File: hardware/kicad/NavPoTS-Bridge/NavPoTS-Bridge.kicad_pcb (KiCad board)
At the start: 2 copper layers, 58.9 x 58.9 mm, 74 parts, among them J1 Conn_01x06_Pin, J2 USB_C_Receptacle_USB2.0_16P, J3 Screw_Terminal_01x06, J4 Conn_02x04_Top_Bottom, J5 Conn_02x04_Top_Bottom, J6 Conn_02x04_Top_Bottom, J7 62684-402100ALF, J8 62684-402100ALF, J9 Conn_02x04_Top_Bottom, U1 MS5611-01BA, U2 H3LIS331DLTR, U3 ASM330LHHXTR, U4 MMC5983MA, U5 USBLC6-2SC6, U6 STM32H743ZITx, Y1 ECS-2520MV-xxx-xx

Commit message: remaped pins and renamed pcb sections
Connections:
- J7 pad 06: EXT_PWR4 -> EXT_PWR2
- J7 pad 07: EXT_PWR5 -> I2C1_SDA
- J7 pad 08: I2C1_SDA -> I2C1_SCL
- J7 pad 09: I2C1_SCL -> PYRO0_FIRE
- J7 pad 10: PYRO0_FIRE -> PYRO0_CONTINUITY
- J7 pad 11: PYRO0_CONTINUITY -> PYRO1_FIRE
- J7 pad 12: PYRO1_FIRE -> PYRO1_CONTINUITY
- J7 pad 13: PYRO1_CONTINUITY -> PYRO2_FIRE
- J7 pad 14: PYRO2_FIRE -> PYRO2_CONTINUITY
- J7 pad 15: PYRO2_CONTINUITY -> PYRO3_FIRE
- J7 pad 16: PYRO3_FIRE -> PYRO3_CONTINUITY
- J7 pad 17: PYRO3_CONTINUITY -> EXT_PWR3
- J7 pad 18: PWM_0 -> EXT_PWR4
- J7 pad 19: PWM_1 -> EXT_PWR5
- J7 pad 20: PWM_2 -> PWM_0
- J7 pad 21: PWM_3 -> PWM_1
- J7 pad 22: PWM_4 -> PWM_2
- J7 pad 23: PWM_5 -> PWM_3
- J7 pad 24: PWM_6 -> PWM_4
- J7 pad 25: PWM_7 -> PWM_5
- J7 pad 26: EXT_PWR2 -> PWM_6
- J7 pad 27: EXT_PWR3 -> PWM_7
- U6 pad 26: unconnected-(U6-PC0-Pad26) -> EXT_PWR3
- U6 pad 27: unconnected-(U6-PC1-Pad27) -> EXT_PWR4
- U6 pad 28: unconnected-(U6-PC2_C-Pad28) -> EXT_PWR5
- U6 pad 56: EXT_PWR2 -> unconnected-(U6-PG0-Pad56)
- U6 pad 57: EXT_PWR3 -> unconnected-(U6-PG1-Pad57)
- U6 pad 7: EXT_PWR4 -> EXT_PWR2
- U6 pad 8: EXT_PWR5 -> unconnected-(U6-PC14-Pad8)

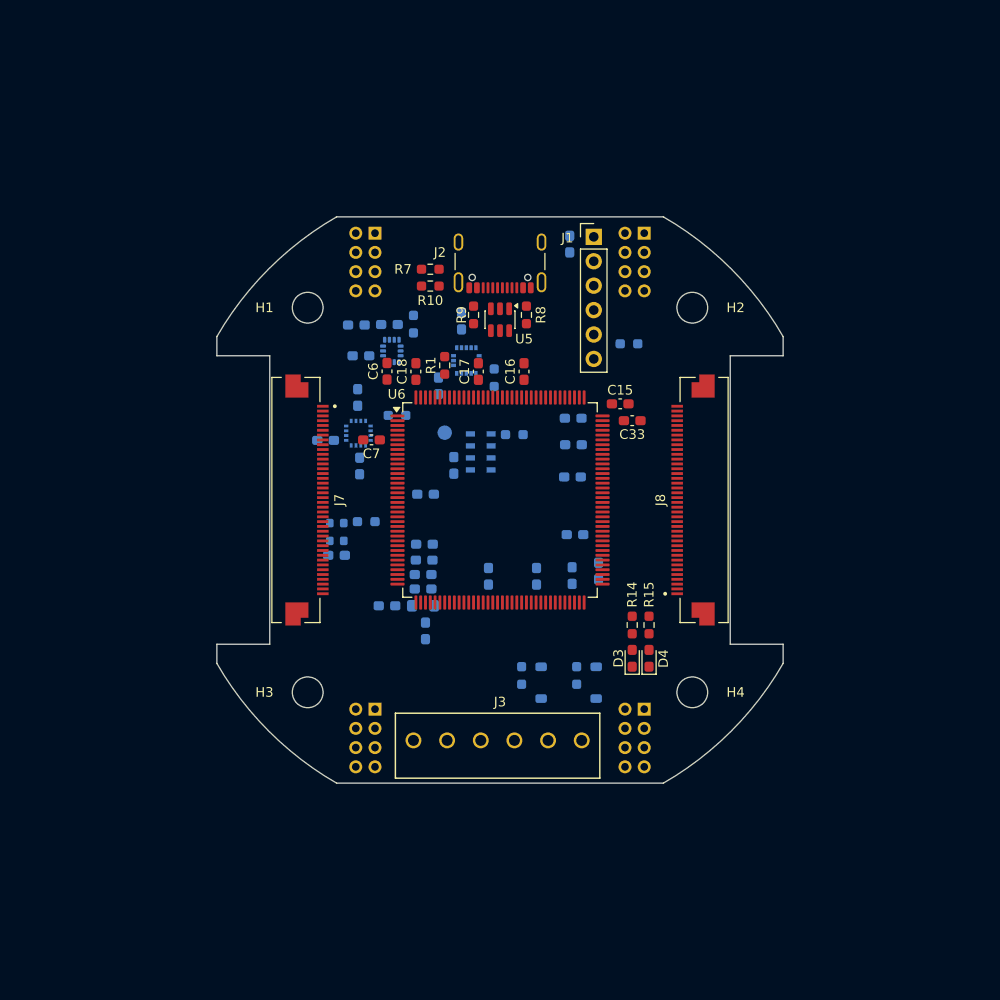
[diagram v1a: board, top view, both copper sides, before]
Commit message: first draft of bridge pcb
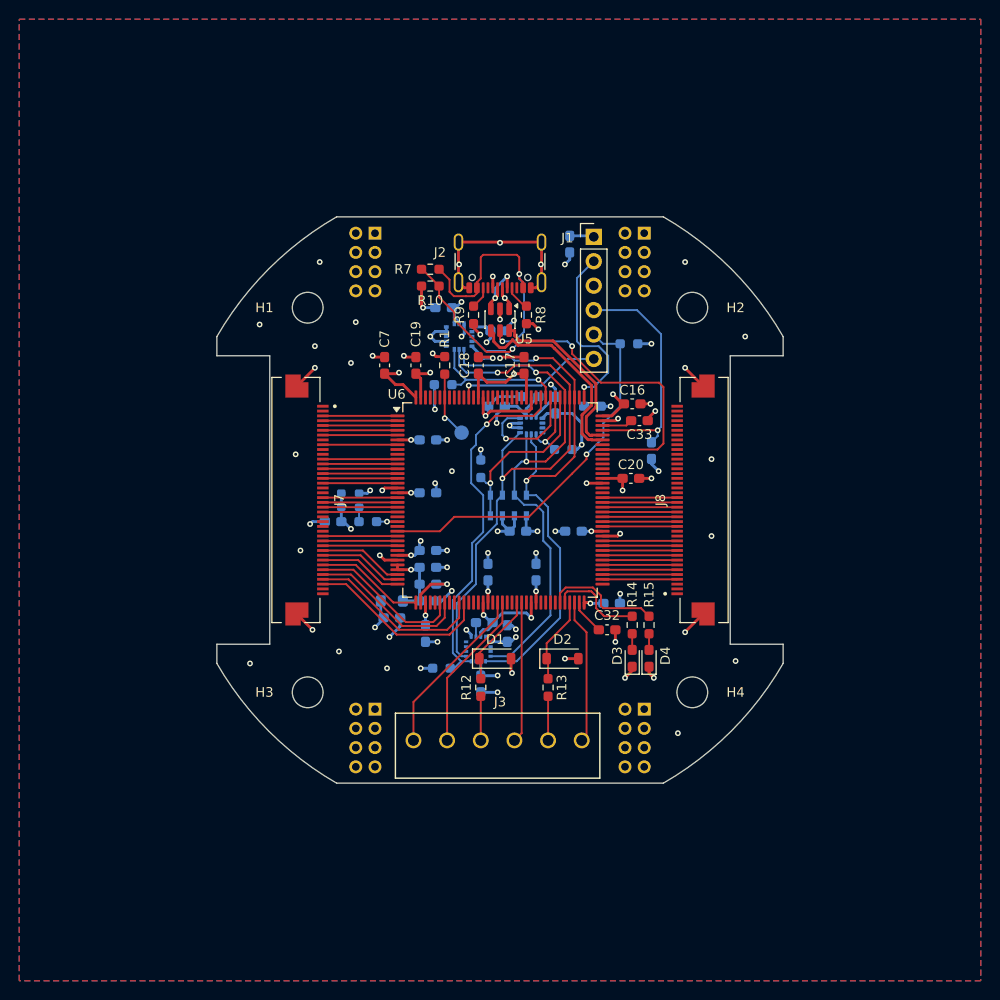
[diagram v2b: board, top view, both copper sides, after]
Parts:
- C20: renamed from C19; moved to F.Cu
- C32, D1, D2, R12, R13: moved to F.Cu
- C8: renamed from C7; moved to B.Cu
- moved C28 32.4 mm to (198.0, 119.1), turned to -90 degrees
- moved C29 27.6 mm to (200.8, 113.9), turned to 90 degrees
- moved R6 26.7 mm to (193.9, 117.5), turned to 0 degrees
- moved U4 25.7 mm to (197.8, 115.5), turned to 90 degrees
- moved C31 20.8 mm to (198.4, 112.8), turned to 0 degrees
- moved R2 20.3 mm to (206.6, 94.8), turned to 180 degrees
- moved C3 19.6 mm to (203.1, 89.2)
- moved C1 19.2 mm to (205.8, 90.1), turned to 90 degrees
- moved U3 16.4 mm to (203.2, 92.2), turned to 0 degrees
- moved C2 15.0 mm to (199.6, 90.2)
- moved C6 9.56 mm to (201.9, 103.2), turned to 180 degrees
- moved C4 8.16 mm to (194.1, 80.0), turned to 180 degrees
- moved C26 8.14 mm to (215.8, 94.9), turned to -90 degrees
- moved C32 6.71 mm to (211.1, 113.5), turned to 180 degrees
- moved U1 6.27 mm to (200.9, 100.6), turned to 90 degrees
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- renumbered C9 to C10, C10 to C11, C11 to C12, C12 to C13, C13 to C14, C14 to C15, C15 to C16, C16 to C17, C17 to C18, C18 to C19, C20 to C21, C21 to C22, C22 to C23, C26 to C25, C27 to C26, C25 to C27, C23 to C6, C6 to C7, C8 to C9
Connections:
- D1 pad 1: UART8_RX -> UART7_RX
- D2 pad 1: UART4_RX -> USART3_TX
- J3 pad 3: UART8_TX -> Net-(J3-Pin_3)
- J3 pad 4: Net-(J3-Pin_4) -> UART7_TX
- J3 pad 5: UART4_TX -> Net-(J3-Pin_5)
- J3 pad 6: Net-(J3-Pin_6) -> USART3_RX
- J7 pad 01: V_ALERT -> unconnected-(J7-Pad01)
- J7 pad 02: PGOOD -> unconnected-(J7-Pad02)
- J7 pad 03: VSTAT -> V_ALERT
- J7 pad 04: EXT_PWR0 -> PGOOD
- J7 pad 05: EXT_PWR1 -> VSTAT
- J7 pad 06: EXT_PWR2 -> EXT_PWR0
- J7 pad 07: I2C1_SDA -> EXT_PWR1
- J7 pad 08: I2C1_SCL -> unconnected-(J7-Pad08)
- J7 pad 09: PYRO0_FIRE -> EXT_PWR2
- J7 pad 10: PYRO0_CONTINUITY -> unconnected-(J7-Pad10)
- J7 pad 11: PYRO1_FIRE -> unconnected-(J7-Pad11)
- J7 pad 12: PYRO1_CONTINUITY -> I2C1_SDA
- J7 pad 13: PYRO2_FIRE -> I2C1_SCL
- J7 pad 14: PYRO2_CONTINUITY -> PYRO0_FIRE
- J7 pad 15: PYRO3_FIRE -> PYRO0_CONTINUITY
- J7 pad 16: PYRO3_CONTINUITY -> PYRO1_FIRE
- J7 pad 17: EXT_PWR3 -> PYRO1_CONTINUITY
- J7 pad 18: EXT_PWR4 -> unconnected-(J7-Pad18)
- J7 pad 19: EXT_PWR5 -> unconnected-(J7-Pad19)
- J7 pad 20: PWM_0 -> PYRO2_FIRE
- J7 pad 21: PWM_1 -> PYRO2_CONTINUITY
- J7 pad 22: PWM_2 -> PYRO3_FIRE
- J7 pad 23: PWM_3 -> PYRO3_CONTINUITY
- J7 pad 24: PWM_4 -> unconnected-(J7-Pad24)
- J7 pad 25: PWM_5 -> unconnected-(J7-Pad25)
- J7 pad 26: PWM_6 -> unconnected-(J7-Pad26)
- J7 pad 27: PWM_7 -> unconnected-(J7-Pad27)
- J7 pad 28: unconnected-(J7-Pad28) -> EXT_PWR3
- J7 pad 29: unconnected-(J7-Pad29) -> EXT_PWR4
- J7 pad 30: unconnected-(J7-Pad30) -> EXT_PWR5
- J7 pad 31: unconnected-(J7-Pad31) -> PWM_0
- J7 pad 32: unconnected-(J7-Pad32) -> PWM_1
- J7 pad 33: unconnected-(J7-Pad33) -> PWM_2
- J7 pad 34: unconnected-(J7-Pad34) -> PWM_3
- J7 pad 35: unconnected-(J7-Pad35) -> PWM_4
- J7 pad 36: unconnected-(J7-Pad36) -> PWM_5
- J7 pad 37: unconnected-(J7-Pad37) -> PWM_6
- J7 pad 38: unconnected-(J7-Pad38) -> PWM_7
- J8 pad 01: SPI2_SCK -> unconnected-(J8-Pad01)
- J8 pad 02: SPI2_MISO -> unconnected-(J8-Pad02)
- J8 pad 03: SPI2_MOSI -> unconnected-(J8-Pad03)
- J8 pad 04: SPI2_CS0 -> SPI2_SCK
- J8 pad 05: SPI2_CS1 -> SPI2_MISO
- J8 pad 06: SPI2_CS2 -> SPI2_MOSI
- J8 pad 07: SPI2_CS3 -> SPI2_CS0
- J8 pad 08: GNSS_nRST -> SPI2_CS1
- J8 pad 09: LoRa_RXEN -> SPI2_CS2
- J8 pad 10: LoRa_BUSY -> SPI2_CS3
- J8 pad 11: LoRa_IO -> GNSS_nRST
- J8 pad 12: LoRa_nRST -> LoRa_RXEN
- J8 pad 13: DEBUG_2 -> unconnected-(J8-Pad13)
- J8 pad 14: DEBUG_3 -> unconnected-(J8-Pad14)
- J8 pad 15: DEBUG_4 -> LoRa_BUSY
- J8 pad 16: DEBUG_5 -> LoRa_IO
- J8 pad 17: unconnected-(J8-Pad17) -> LoRa_nRST
- J8 pad 18: unconnected-(J8-Pad18) -> DEBUG_2
- J8 pad 19: unconnected-(J8-Pad19) -> DEBUG_3
- J8 pad 20: unconnected-(J8-Pad20) -> DEBUG_4
- J8 pad 21: unconnected-(J8-Pad21) -> DEBUG_5
- R12 pad 1: UART8_RX -> UART7_RX
- R12 pad 2: Net-(J3-Pin_4) -> Net-(J3-Pin_3)
- R13 pad 1: UART4_RX -> USART3_TX
- R13 pad 2: Net-(J3-Pin_6) -> Net-(J3-Pin_5)
- U6 pad 124: DEBUG_0 -> unconnected-(U6-PG9-Pad124)
- U6 pad 125: DEBUG_1 -> unconnected-(U6-PG10-Pad125)
- U6 pad 136: I2C4_SCL -> unconnected-(U6-PB6-Pad136)
- U6 pad 137: I2C4_SDA -> unconnected-(U6-PB7-Pad137)
- U6 pad 139: UART4_RX -> unconnected-(U6-PB8-Pad139)
- U6 pad 140: UART4_TX -> unconnected-(U6-PB9-Pad140)
- U6 pad 141: UART8_RX -> unconnected-(U6-PE0-Pad141)
- U6 pad 142: UART8_TX -> unconnected-(U6-PE1-Pad142)
- U6 pad 54: unconnected-(U6-PF14-Pad54) -> I2C4_SCL
- U6 pad 55: unconnected-(U6-PF15-Pad55) -> I2C4_SDA
- U6 pad 58: unconnected-(U6-PE7-Pad58) -> UART7_RX
- U6 pad 59: unconnected-(U6-PE8-Pad59) -> UART7_TX
- U6 pad 67: unconnected-(U6-PE14-Pad67) -> DEBUG_1
- U6 pad 68: unconnected-(U6-PE15-Pad68) -> DEBUG_0
- U6 pad 69: unconnected-(U6-PB10-Pad69) -> USART3_TX
- U6 pad 70: unconnected-(U6-PB11-Pad70) -> USART3_RX
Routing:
- net GND: track 0.00 -> 144.1 mm, vias 0 -> 75
- net +3V3: track 0.00 -> 96.3 mm, vias 0 -> 27
- net SPI3_SCK: track 0.00 -> 57.9 mm, vias 0 -> 2
- net SPI3_MISO: track 0.00 -> 56.3 mm, vias 0 -> 2
- net SPI3_MOSI: track 0.00 -> 53.3 mm, vias 0 -> 2
- net VUSB: track 0.00 -> 45.2 mm, vias 0 -> 2
- net NRST: track 0.00 -> 39.4 mm, vias 0 -> 1
- net SPI3_CS3: track 0.00 -> 37.4 mm, vias 0 -> 1
- net Net-(U5-VBUS): track 0.00 -> 27.5 mm, vias 0 -> 2
- net SWDIO: track 0.00 -> 25.4 mm, vias 0 -> 1
- net USB_D-: track 0.00 -> 21.8 mm
- net SWCLK: track 0.00 -> 20.9 mm, vias 0 -> 1
- net PWM_7: track 0.00 -> 19.3 mm
- net USB_D+: track 0.00 -> 18.9 mm
- net SPI3_CS0: track 0.00 -> 18.6 mm, vias 0 -> 1
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- added copper zone on In2.Cu, net +3V3
- added copper zone on B.Cu, net GND
- added copper zone on F.Cu, net GND
- added copper zone on In1.Cu, net GND
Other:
- copper layers 2 -> 4

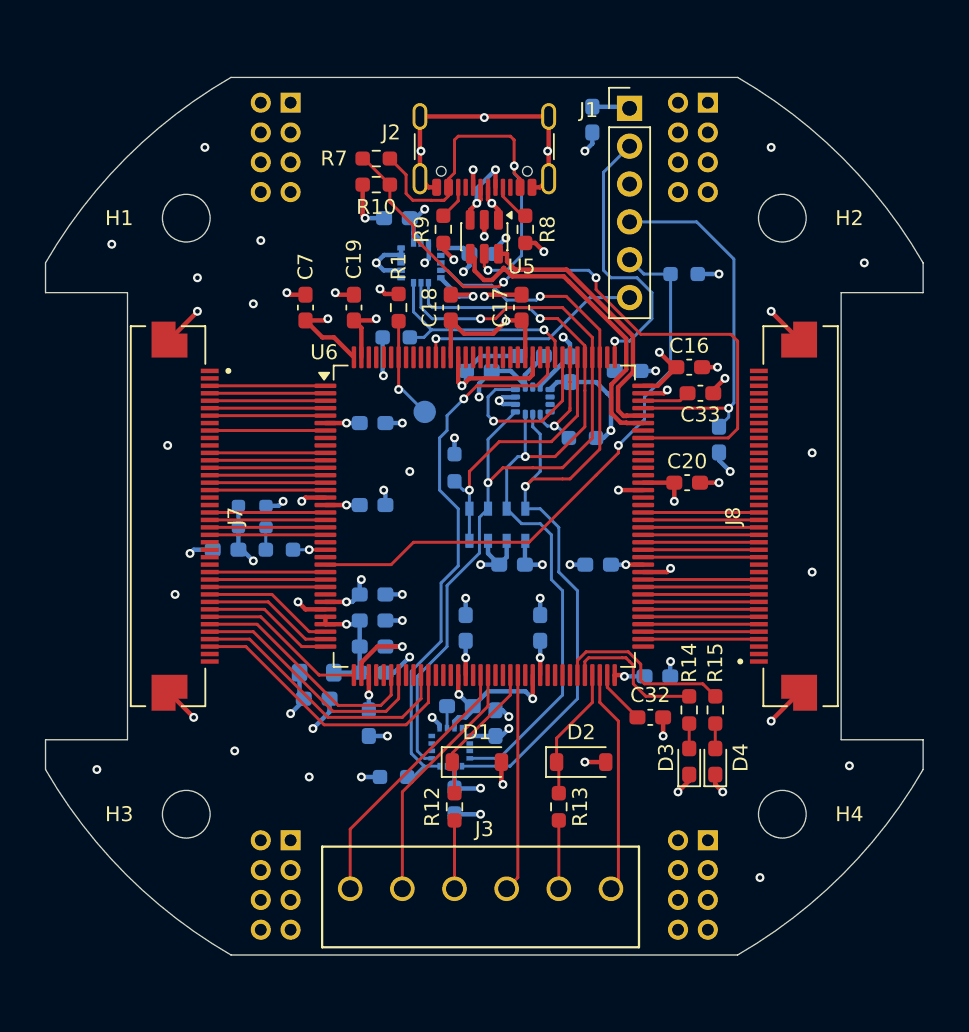
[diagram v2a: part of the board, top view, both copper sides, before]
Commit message: first draft of south board layout and high current traces
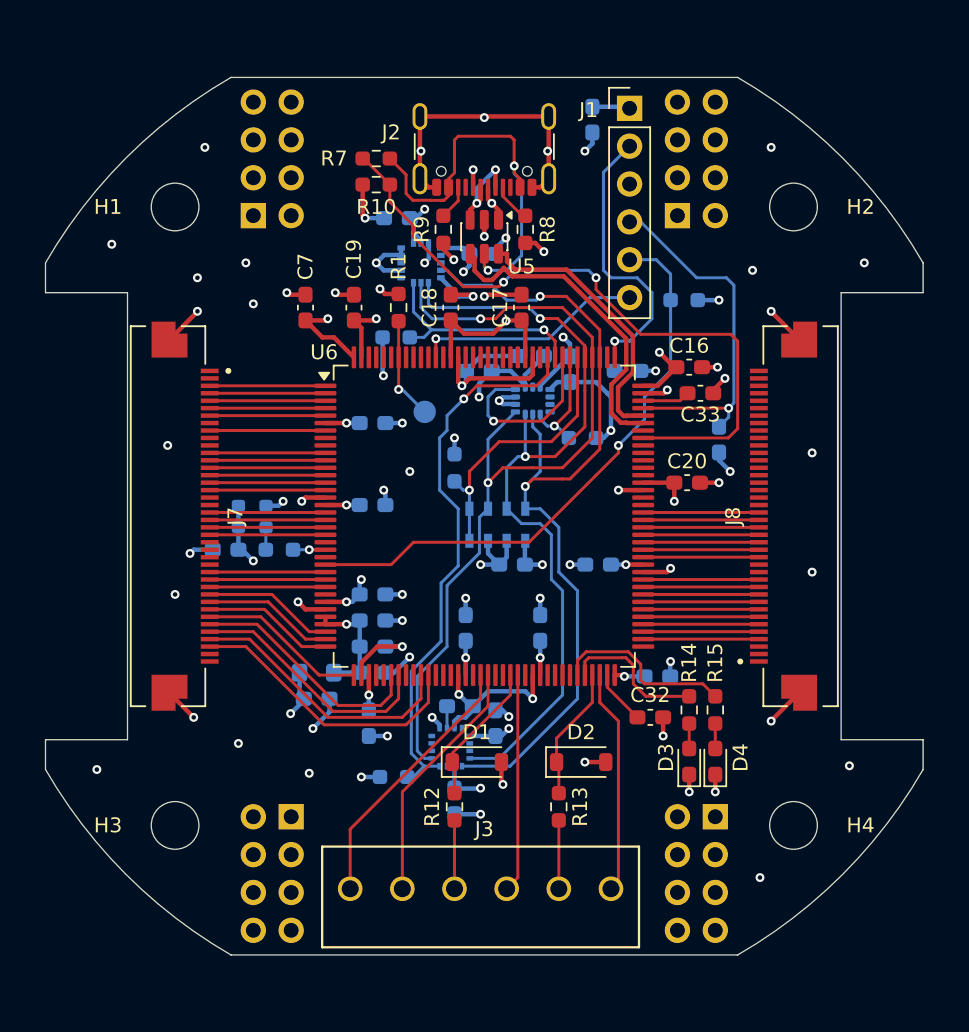
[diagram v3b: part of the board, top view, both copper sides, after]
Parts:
- J4, J5, J6, J9: footprint Connector_PinHeader_2.00mm:PinHeader_2x04_P2.00mm_Vertical -> Connector_PinHeader_2.54mm:PinHeader_2x04_P2.54mm_Vertical
- moved J6 7.98 mm to (184.5, 79.8), turned to 0 degrees
- moved J9 7.85 mm to (213.0, 79.8), turned to 0 degrees
- moved R5 1.75 mm to (213.4, 85.5)
- moved J4 1.66 mm to (215.5, 120.2)
- moved J5 1.58 mm to (187.0, 120.2)
- moved H1 1.06 mm to (179.2, 79.2)
- moved H2 1.06 mm to (220.8, 79.2)
- moved H3 1.06 mm to (179.2, 120.8)
- moved H4 1.06 mm to (220.8, 120.8)
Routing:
- net SWDIO: track 25.4 -> 24.4 mm
- net GND: track 144.1 -> 143.6 mm, vias 75 -> 76

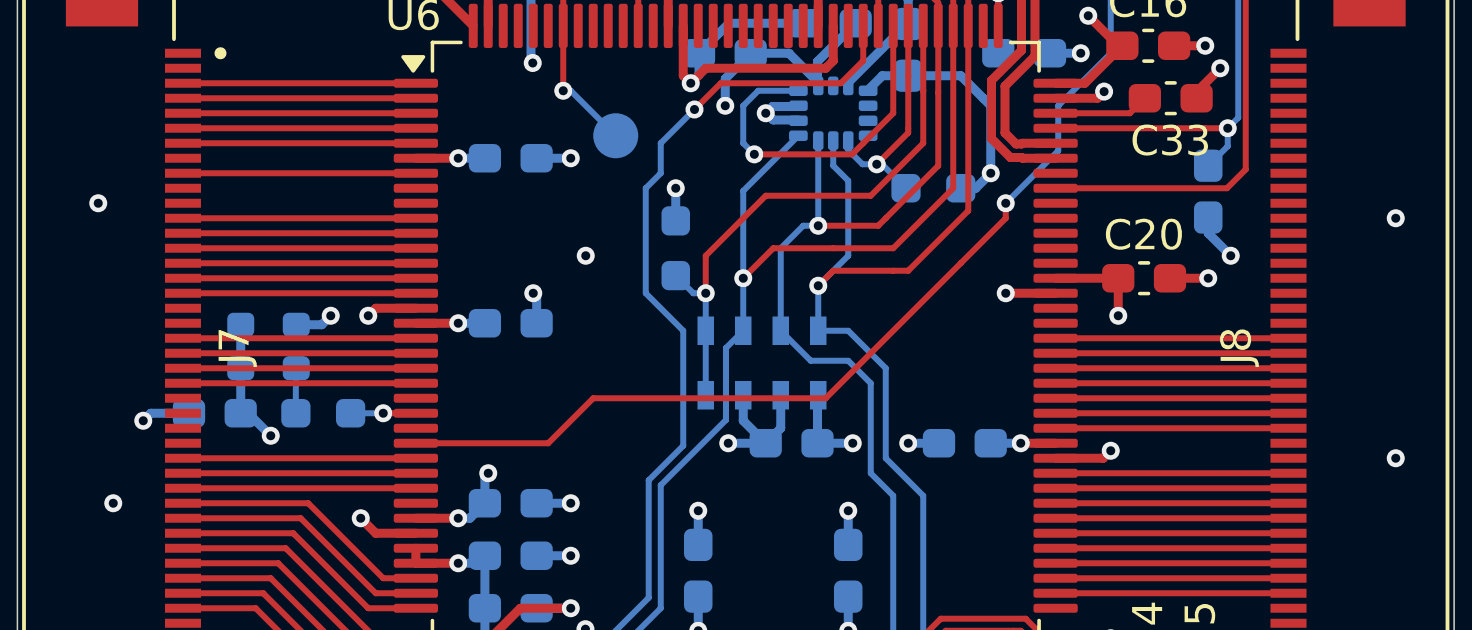
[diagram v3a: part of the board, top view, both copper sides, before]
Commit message: added gpio for future use on north and south boards
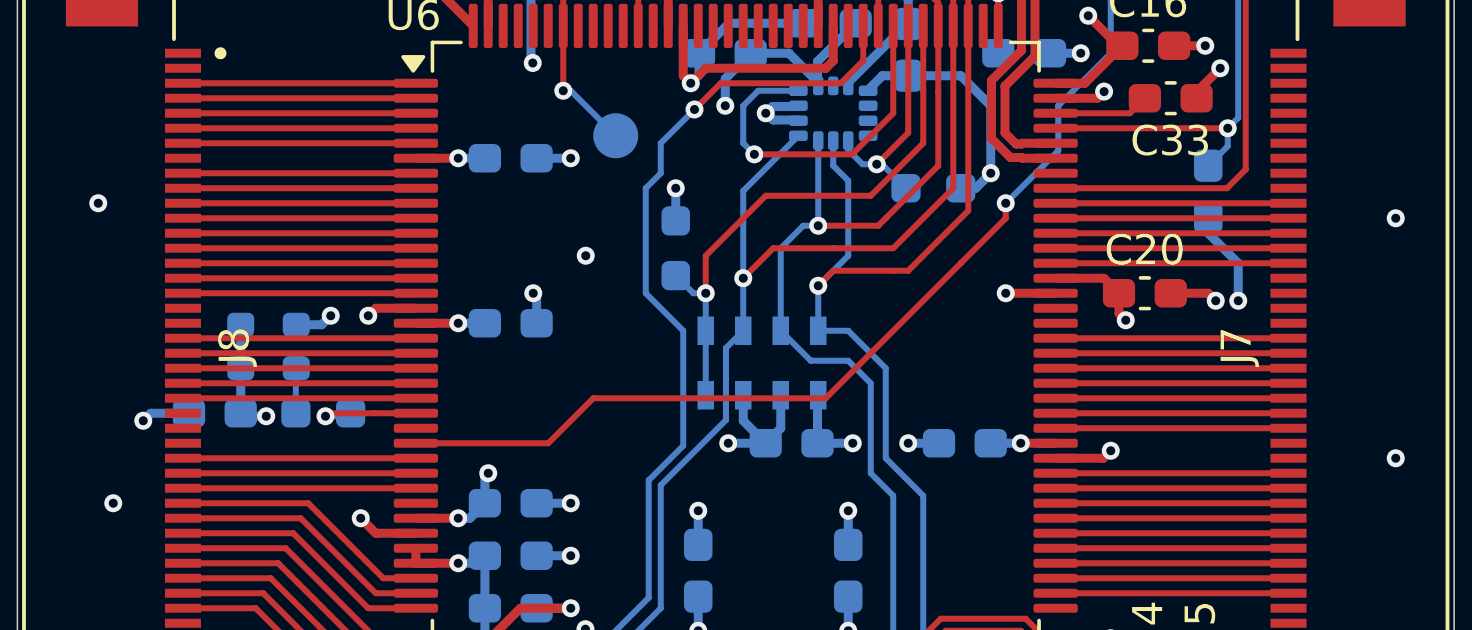
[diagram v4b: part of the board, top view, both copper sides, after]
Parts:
- removed the J7 at (178.0, 100.0)
- added J8: 62684-402100ALF, custom:Amphenol_62684-402100ALF, F.Cu at (178.0, 100.0)
- moved C20 0.50 mm to (213.6, 98.2)
- renumbered J8 to J7
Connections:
- J7 pad 26: unconnected-(J8-Pad26) -> EXT_PWR2
- J7 pad 27: unconnected-(J8-Pad27) -> EXT_PWR3
- J7 pad 28: unconnected-(J8-Pad28) -> GPIO_7
- J7 pad 29: unconnected-(J8-Pad29) -> GPIO_8
- J7 pad 30: unconnected-(J8-Pad30) -> GPIO_9
- U6 pad 100: unconnected-(U6-PA8-Pad100) -> GPIO_9
- U6 pad 22: unconnected-(U6-PF10-Pad22) -> GPIO_5
- U6 pad 26: EXT_PWR3 -> GPIO_6
- U6 pad 27: EXT_PWR4 -> EXT_PWR1
- U6 pad 28: EXT_PWR5 -> EXT_PWR0
- U6 pad 4: EXT_PWR0 -> GPIO_0
- U6 pad 5: EXT_PWR1 -> GPIO_1
- U6 pad 7: EXT_PWR2 -> GPIO_2
- U6 pad 8: unconnected-(U6-PC14-Pad8) -> GPIO_3
- U6 pad 9: unconnected-(U6-PC15-Pad9) -> GPIO_4
- U6 pad 96: unconnected-(U6-PC6-Pad96) -> EXT_PWR2
- U6 pad 97: unconnected-(U6-PC7-Pad97) -> EXT_PWR3
- U6 pad 98: unconnected-(U6-PC8-Pad98) -> GPIO_7
- U6 pad 99: unconnected-(U6-PC9-Pad99) -> GPIO_8
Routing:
- net GPIO_9: track 0.00 -> 7.76 mm
- net GPIO_8: track 0.00 -> 7.76 mm
- net GPIO_7: track 0.00 -> 7.76 mm
- net GPIO_6: track 0.00 -> 7.76 mm
- net GPIO_5: track 0.00 -> 7.76 mm
- net GPIO_4: track 0.00 -> 7.76 mm
- net GPIO_3: track 0.00 -> 7.76 mm
- net GPIO_2: track 0.00 -> 7.76 mm
- net GPIO_1: track 0.00 -> 7.76 mm
- net GPIO_0: track 0.00 -> 7.76 mm
- net EXT_PWR5: track 7.76 -> 0.00 mm
- net EXT_PWR4: track 7.76 -> 0.00 mm
- net HSE_IN: track 2.17 -> 4.27 mm
- net GND: track 143.6 -> 145.5 mm
